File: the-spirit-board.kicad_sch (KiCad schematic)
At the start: 0 parts

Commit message: Initial commit of the schematic and board files with the ESP32
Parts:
- added IC1: ESP32-C6-WROOM-1-N8, TheSPIRITBoard:ESP32C6WROOM1N8, symbol TheSPIRITBoard:ESP32-C6-WROOM-1-N8
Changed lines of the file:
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@@
 	(generator_version "9.0")
 	(paper "A4")
+	(symbol
+		(lib_id "TheSPIRITBoard:ESP32-C6-WROOM-1-N8")
+		(at 116.84 58.42 0)
+		(unit 1)
+		(exclude_from_sim no)
+		(in_bom yes)
+		(on_board yes)
+		(dnp no)
+		(fields_autoplaced yes)
+		(property "Reference" "IC1"
+			(at 133.35 50.8 0)
+			(effects
+				(font
+					(size 1.27 1.27)
+				)
+			)
+		)
+		(property "Value" "ESP32-C6-WROOM-1-N8"
+			(at 133.35 53.34 0)
+			(effects
+				(font
+					(size 1.27 1.27)
+				)
+			)
+		)
+		(property "Footprint" "TheSPIRITBoard:ESP32C6WROOM1N8"
+			(at 146.05 55.88 0)
+			(effects
+				(font
+					(size 1.27 1.27)
+				)
+				(justify left)
+				(hide yes)
+			)
+		)
+		(property "Datasheet" "https://www.espressif.com/sites/default/files/documentation/esp32-c6-wroom-1_datasheet_en.pdf"
+			(at 146.05 58.42 0)
+			(effects
+				(font
+					(size 1.27 1.27)
+				)
+				(justify left)
+				(hide yes)
+			)
+		)
+		(property "Description" ""
+			(at 116.84 58.42 0)
+			(effects
+				(font
+					(size 1.27 1.27)
+				)
+				(hide yes)
+			)
+		)
+		(property "Description_1" "802.15.4, Bluetooth, WiFi Bluetooth v5.0, Zigbee Transceiver Module 2.4GHz PCB Trace Surface Mount"
+			(at 146.05 60.96 0)
+			(effects
+				(font
+					(size 1.27 1.27)
+				)
+				(justify left)
+				(hide yes)
+			)
+		)
+		(property "Height" "3.25"
+			(at 146.05 63.5 0)
+			(effects
+				(font
+					(size 1.27 1.27)
+				)
+				(justify left)
+				(hide yes)
+			)
+		)
+		(property "Mouser Part Number" "356-ESP32C6WROOM1N8"
+			(at 146.05 66.04 0)
+			(effects
+				(font
+					(size 1.27 1.27)
+				)
+				(justify left)
+				(hide yes)
+			)
+		)
+		(property "Mouser Price/Stock" "https://www.mouser.co.uk/ProductDetail/Espressif-Systems/ESP32-C6-WROOM-1-N8?qs=8Wlm6%252BaMh8ST02Gmwp74cw%3D%3D"
+			(at 146.05 68.58 0)
+			(effects
+				(font
+					(size 1.27 1.27)
+				)
+				(justify left)
+				(hide yes)
+			)
+		)
+		(property "Manufacturer_Name" "Espressif Systems"
+			(at 146.05 71.12 0)
+			(effects
+				(font
+					(size 1.27 1.27)
+				)
+				(justify left)
+				(hide yes)
+			)
+		)
+		(property "Manufacturer_Part_Number" "ESP32-C6-WROOM-1-N8"
+			(at 146.05 73.66 0)
+			(effects
+				(font
+					(size 1.27 1.27)
+				)
+				(justify left)
+				(hide yes)
+			)
+		)
+		(pin "4"
+		)
+		(pin "7"
+		)
+		(pin "5"
+		)
+		(pin "11"
+		)
+		(pin "9"
+		)
+		(pin "1"
+		)
+		(pin "2"
+		)
+		(pin "3"
+		)
+		(pin "6"
+		)
+		(pin "8"
+		)
+		(pin "10"
+		)
+		(pin "25"
+		)
+		(pin "21"
+		)
+		(pin "31"
+		)
+		(pin "20"
+		)
+		(pin "16"
+		)
+		(pin "14"
+		)
+		(pin "12"
+		)
+		(pin "22"
+		)
+		(pin "27"
+		)
+		(pin "28"
+		)
+		(pin "29"
+		)
+		(pin "32"
+		)
+		(pin "23"
+		)
+		(pin "33"
+		)
+		(pin "17"
+		)
+		(pin "34"
+		)
+		(pin "13"
+		)
+		(pin "18"
+		)
+		(pin "24"
+		)
+		(pin "19"
+		)
+		(pin "15"
+		)
+		(pin "26"
+		)
+		(pin "30"
+		)
+		(pin "35"
+		)
+		(pin "36"
+		)
+		(pin "37"
+		)
+		(instances
+			(project ""
+				(path "/647d8e4d-af54-40e7-b6a4-72dcab194c10"
+					(reference "IC1")
+					(unit 1)
+				)
+			)
+		)
+	)
 	(sheet_instances
 		(path "/"

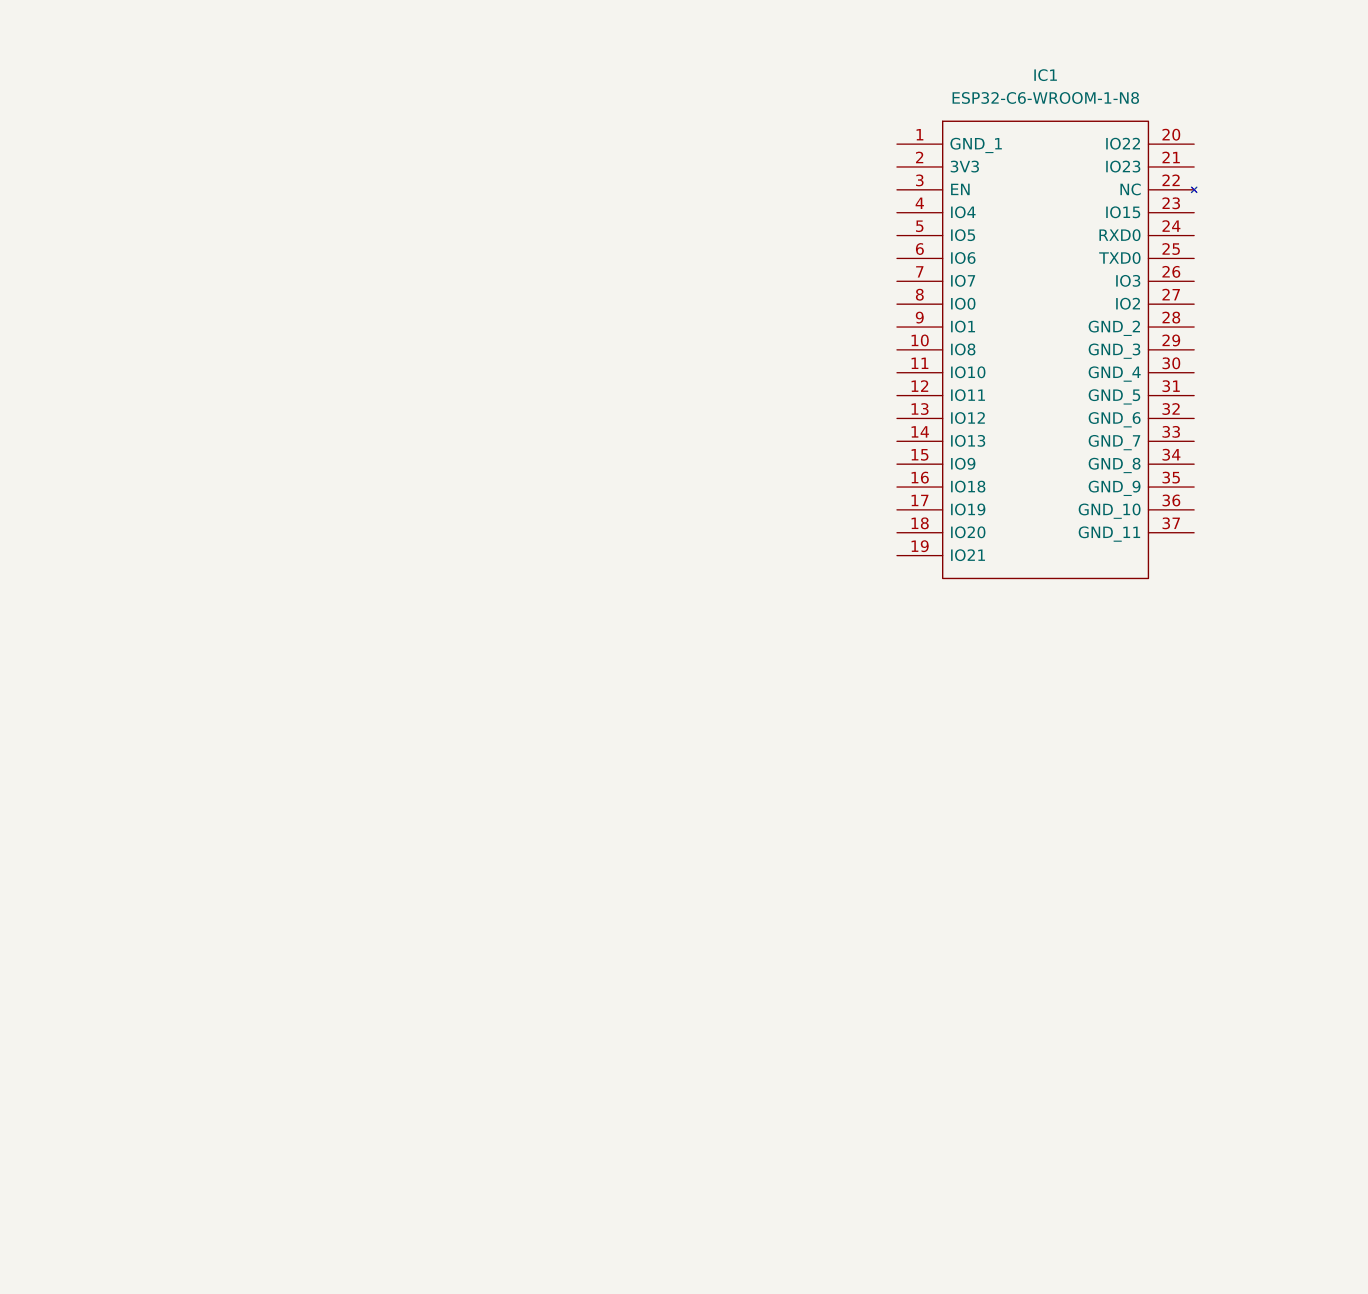
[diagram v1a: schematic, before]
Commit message: Add power supply and momentary switch for enable
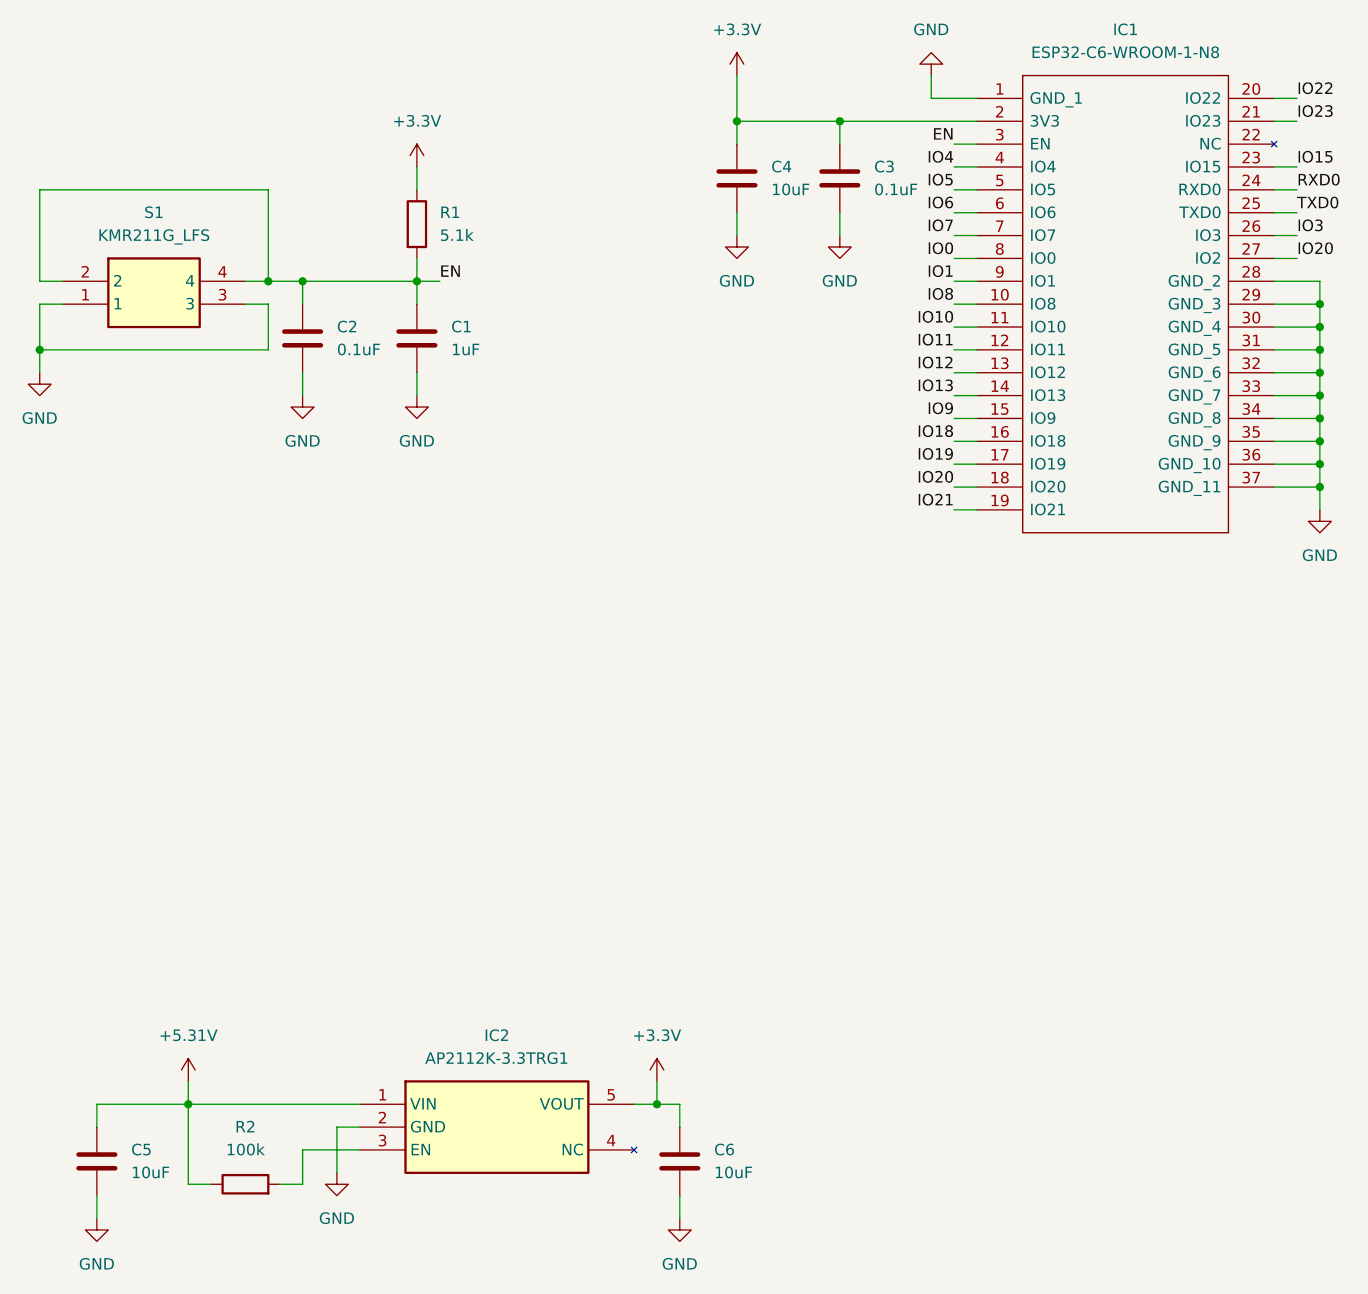
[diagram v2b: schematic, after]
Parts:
- added C1: 1uF, Capacitor_SMD:C_0603_1608Metric, symbol Device:C
- added C2, C3: 0.1uF, Capacitor_SMD:C_0402_1005Metric, symbol Device:C
- added C4, C5, C6: 10uF, Capacitor_SMD:C_0603_1608Metric, symbol Device:C
- added IC2: AP2112K-3.3TRG1, TheSPIRITBoard:SOT95P285X140-5N, symbol TheSPIRITBoard:AP2112K-3.3TRG1
- added R1: 5.1k, Resistor_SMD:R_0603_1608Metric, symbol Device:R
- added R2: 100k, Resistor_SMD:R_0603_1608Metric, symbol Device:R
- added S1: KMR211G_LFS, TheSPIRITBoard:KMR_2, symbol TheSPIRITBoard:KMR211G_LFS
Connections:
- net GND: now reaches IC1.1 (GND_1)
- net GND: now also IC1.28 (GND_2), IC1.29 (GND_3), IC1.30 (GND_4), IC1.31 (GND_5), IC1.32 (GND_6), IC1.33 (GND_7), IC1.34 (GND_8), IC1.35 (GND_9), IC1.36 (GND_10), IC1.37 (GND_11), C1.2, C2.2, C3.2, C4.2, C5.1, C6.1, IC2.2 (GND), S1.1, S1.3
- net IO8: now reaches IC1.10 (IO8)
- net IO10: now reaches IC1.11 (IO10)
- net IO11: now reaches IC1.12 (IO11)
- net IO12: now reaches IC1.13 (IO12)
- net IO13: now reaches IC1.14 (IO13)
- net IO9: now reaches IC1.15 (IO9)
- net IO18: now reaches IC1.16 (IO18)
- net IO19: now reaches IC1.17 (IO19)
- net IO20: now reaches IC1.18 (IO20)
- net IO20: now also IC1.27 (IO2)
- net IO21: now reaches IC1.19 (IO21)
- net +3.3V: now reaches IC1.2 (3V3)
- net +3.3V: now also C3.1, C4.1, C6.2, IC2.5 (VOUT), R1.1
- net IO22: now reaches IC1.20 (IO22)
- net IO23: now reaches IC1.21 (IO23)
- net IO15: now reaches IC1.23 (IO15)
- net RXD0: now reaches IC1.24 (RXD0)
- net TXD0: now reaches IC1.25 (TXD0)
- net IO3: now reaches IC1.26 (IO3)
- net EN: now reaches IC1.3 (EN)
- net EN: now also C1.1, C2.1, R1.2, S1.2, S1.4
- net IO4: now reaches IC1.4 (IO4)
- net IO5: now reaches IC1.5 (IO5)
- net IO6: now reaches IC1.6 (IO6)
- net IO7: now reaches IC1.7 (IO7)
- net IO0: now reaches IC1.8 (IO0)
- net IO1: now reaches IC1.9 (IO1)
- new net: IC2.3 (EN), R2.2
- new net +5.31V: C5.2, IC2.1 (VIN), R2.1
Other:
- moved on the sheet: IC1

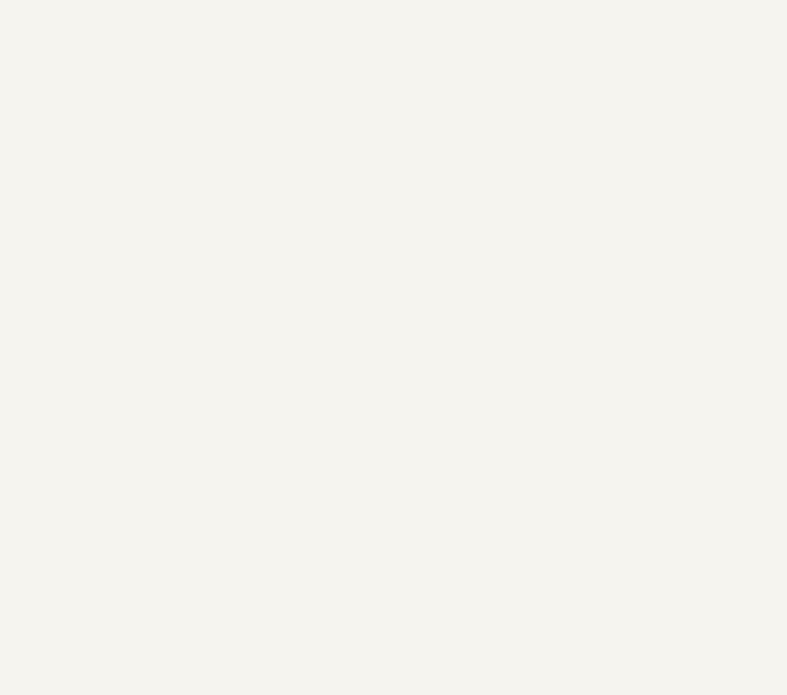
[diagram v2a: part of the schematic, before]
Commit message: Add the footprint for the Furby and do initial connections
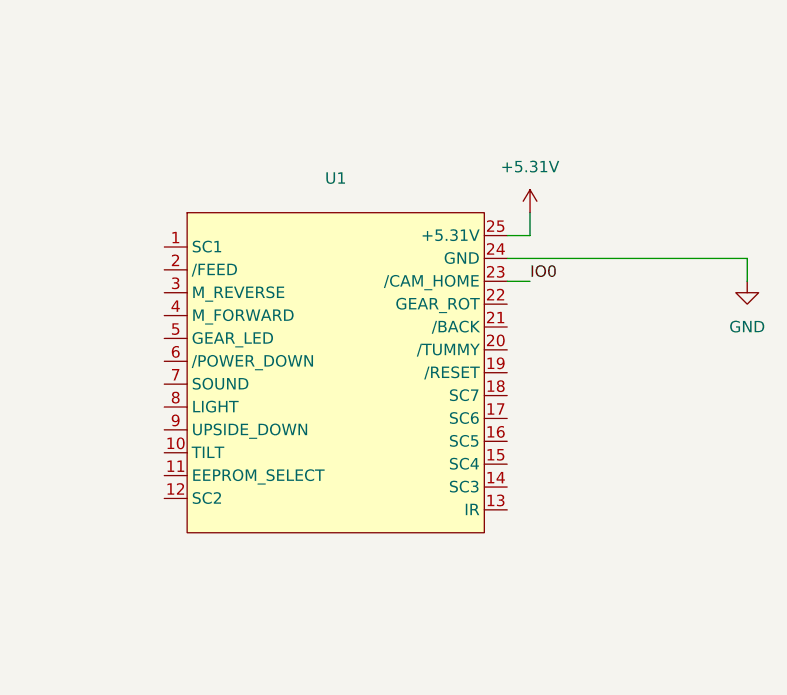
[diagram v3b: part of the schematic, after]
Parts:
- added U1: ~, TheSPIRITBoard:FURBY, symbol TheSPIRITBoard:FURBY
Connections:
- net +5.31V: now also U1.25 (+5.31V)
- net GND: now also U1.24 (GND)
- net IO0: now also U1.23 (/CAM_HOME)

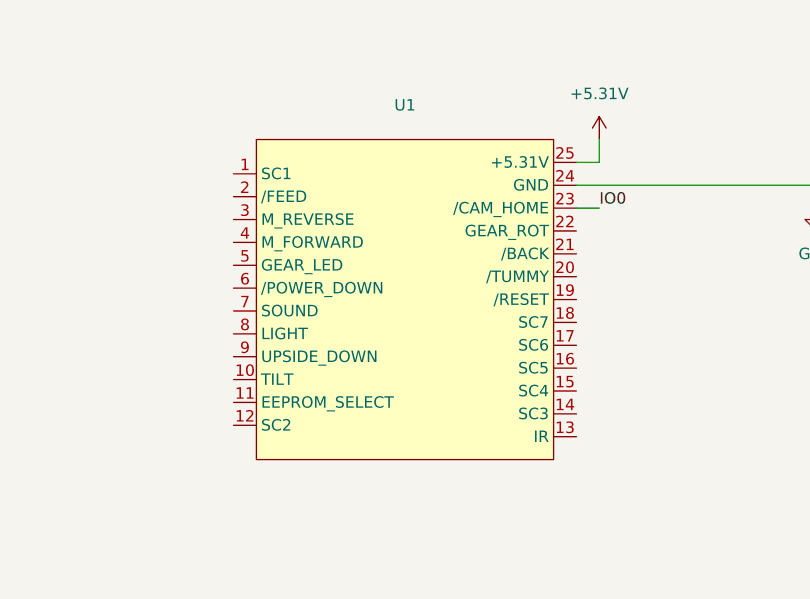
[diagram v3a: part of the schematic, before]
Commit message: Update the schematic symbol for the Furby main board connection
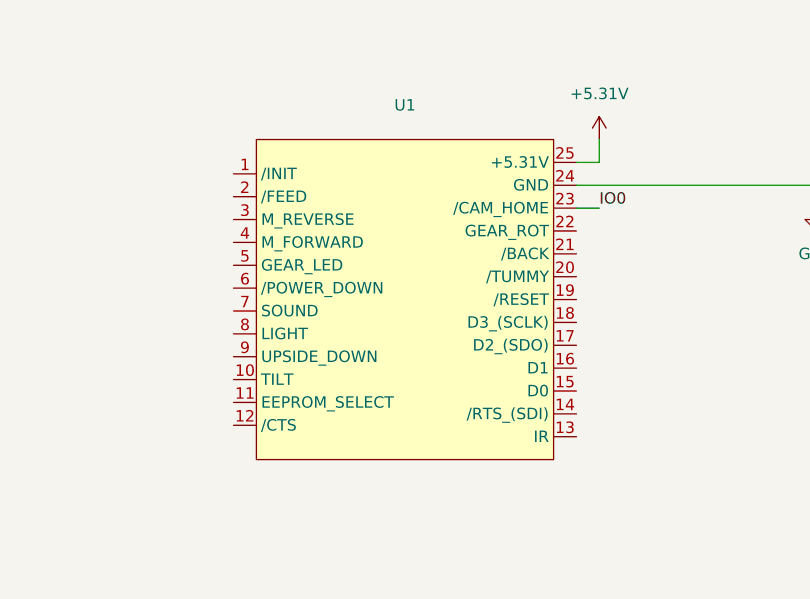
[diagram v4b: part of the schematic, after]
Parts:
- IC1: footprint TheSPIRITBoard:ESP32C6WROOM1N8 -> ESP32C6WROOM1N8
- IC2: footprint TheSPIRITBoard:SOT95P285X140-5N -> SOT95P285X140-5N
- S1: footprint TheSPIRITBoard:KMR_2 -> KMR_2
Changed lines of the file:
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@@
 			)
 		)
-		(property "Footprint" "TheSPIRITBoard:SOT95P285X140-5N"
+		(property "Footprint" "SOT95P285X140-5N"
 			(at 83.82 260.02 0)
 			(effects
@@
 			)
 		)
-		(property "Footprint" "TheSPIRITBoard:KMR_2"
+		(property "Footprint" "KMR_2"
 			(at 40.64 168.58 0)
 			(effects
@@
 			)
 		)
-		(property "Footprint" "TheSPIRITBoard:ESP32C6WROOM1N8"
+		(property "Footprint" "ESP32C6WROOM1N8"
 			(at 154.94 50.8 0)
 			(effects
